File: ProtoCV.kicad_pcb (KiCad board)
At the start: 2 copper layers, 100 x 100 mm, 142 parts, among them J1 AudioJack2_SwitchT, J10 Conn_01x01_Male, J11 Conn_01x05_Male, J12 Conn_01x09_Male, J13 AudioJack2_SwitchT, J14 AudioJack2_SwitchT, J15 AudioJack2_SwitchT, J16 AudioJack2_SwitchT, J17 AudioJack2_SwitchT, J18 AudioJack2_SwitchT, J19 AudioJack2_SwitchT, J2 AudioJack2_SwitchT, J20 AudioJack2_SwitchT, J21 Conn_01x01_Male, J22 Conn_01x01_Male, J23 Conn_01x01_Male, J24 Conn_01x01_Male, J25 Conn_01x01_Male, J26 Conn_01x01_Male, J27 Conn_01x01_Male, J28 Conn_01x01_Male, J29 Conn_01x01_Male, J3 AudioJack2_SwitchT, J30 Conn_01x01_Male, J4 AudioJack2_SwitchT, J5 AudioJack2_SwitchT, J6 AudioJack2_SwitchT, J7 AudioJack2_SwitchT, J8 AudioJack2_SwitchT, J9 Conn_02x05_Odd_Even, Q1 BC847, Q2 BC847, Q3 BC847, Q4 BC847, Q5 BC847, Q6 BC847, Q7 BC847, Q8 BC847, U1 OPA4192, U2 OPA4192, U3 ADC80508Z, U4 R-78E3.3-0.5, U5 LD2981ABU33TR, U6 74AHCT244, U7 L7805

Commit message: Corrected led resistor values.
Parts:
- R36, R37, R38, R39, R40, R41, R42, R43: value 47 -> 330
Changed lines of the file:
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@@
   )
   (setup
-    (last_trace_width 0.254)
+    (last_trace_width 0.25)
     (user_trace_width 0.254)
     (user_trace_width 0.381)
@@
       (effects (font (size 1 1) (thickness 0.15)))
     )
-    (fp_text value 47 (at 0 1.43) (layer F.Fab)
+    (fp_text value 330 (at 0 1.43) (layer F.Fab)
       (effects (font (size 1 1) (thickness 0.15)))
     )
@@
       (effects (font (size 1 1) (thickness 0.15)))
     )
-    (fp_text value 47 (at 0 1.43) (layer F.Fab)
+    (fp_text value 330 (at 0 1.43) (layer F.Fab)
       (effects (font (size 1 1) (thickness 0.15)))
     )
@@
       (effects (font (size 1 1) (thickness 0.15)))
     )
-    (fp_text value 47 (at 0 1.43) (layer F.Fab)
+    (fp_text value 330 (at 0 1.43) (layer F.Fab)
       (effects (font (size 1 1) (thickness 0.15)))
     )
@@
       (effects (font (size 1 1) (thickness 0.15)))
     )
-    (fp_text value 47 (at 0 1.43) (layer F.Fab)
+    (fp_text value 330 (at 0 1.43) (layer F.Fab)
       (effects (font (size 1 1) (thickness 0.15)))
     )
@@
       (effects (font (size 1 1) (thickness 0.15)))
     )
-    (fp_text value 47 (at 0 1.43) (layer F.Fab)
+    (fp_text value 330 (at 0 1.43) (layer F.Fab)
       (effects (font (size 1 1) (thickness 0.15)))
     )
@@
       (effects (font (size 1 1) (thickness 0.15)))
     )
-    (fp_text value 47 (at 0 1.43) (layer F.Fab)
+    (fp_text value 330 (at 0 1.43) (layer F.Fab)
       (effects (font (size 1 1) (thickness 0.15)))
     )
@@
       (effects (font (size 1 1) (thickness 0.15)))
     )
-    (fp_text value 47 (at 0 1.43) (layer F.Fab)
+    (fp_text value 330 (at 0 1.43) (layer F.Fab)
       (effects (font (size 1 1) (thickness 0.15)))
     )
@@
       (effects (font (size 1 1) (thickness 0.15)))
     )
-    (fp_text value 47 (at 0 1.43) (layer F.Fab)
-      (effects (font (size 1 1) (thickness 0.15)))
-    )
+    (fp_text value 330 (at 0 1.43) (layer F.Fab)
+      (effects (font (size 1 1) (thickness 0.15)))
+    )

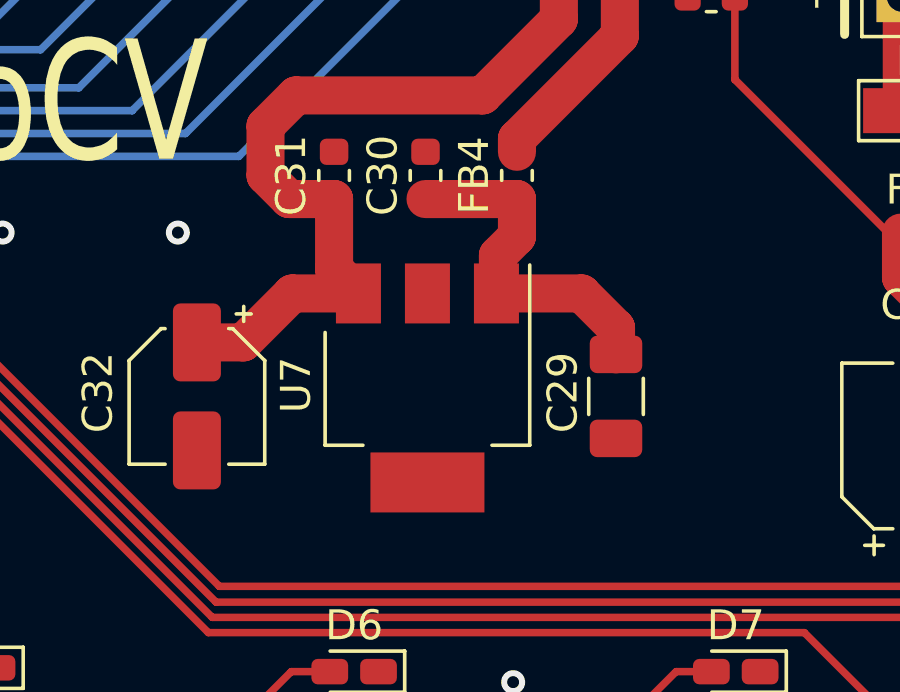
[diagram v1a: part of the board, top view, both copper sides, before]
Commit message: Corrected footprint for 5V regulator.
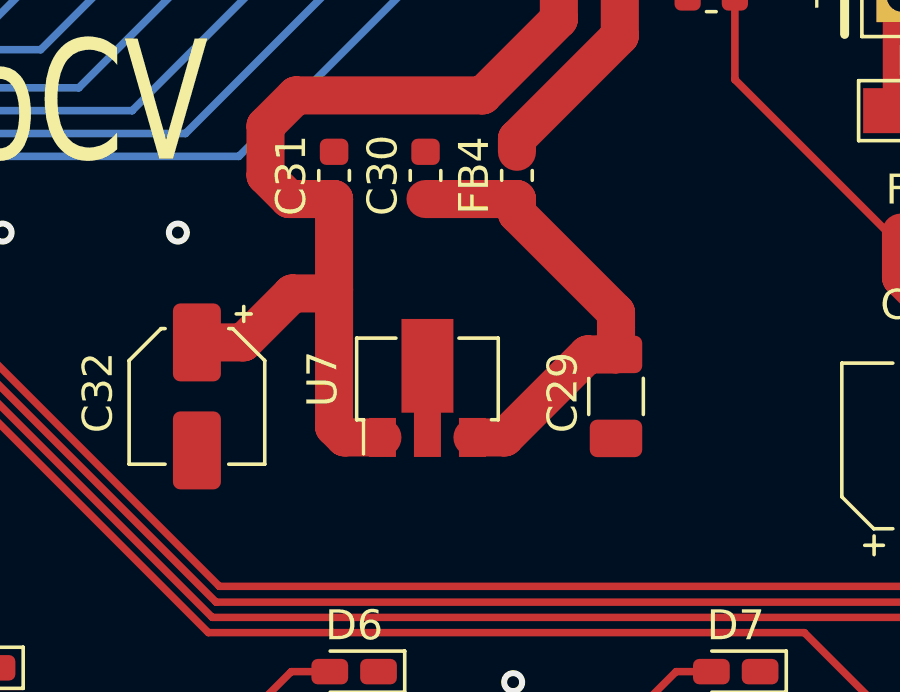
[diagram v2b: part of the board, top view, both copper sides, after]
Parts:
- U7: value L7805 -> L78L05_SOT89; footprint Package_TO_SOT_SMD:SOT-223-3_TabPin2 -> Package_TO_SOT_SMD:SOT-89-3
- turned U7 to 90 degrees
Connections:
- U7 pad 1: Net-(C29-Pad1) -> +5V
- U7 pad 3: +5V -> Net-(C29-Pad1)
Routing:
- net +5V: track 85.4 -> 90.5 mm
- net Net-(C29-Pad1): track 11.8 -> 15.5 mm
